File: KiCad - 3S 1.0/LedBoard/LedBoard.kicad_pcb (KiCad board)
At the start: 2 copper layers, 34 x 31.7 mm, 15 parts, among them J1 Conn_01x02, SW1 SW_SPST, U1 TPS565208

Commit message: Finished up LED PCB and made some small tweaks and fixes to main board.
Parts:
- added G***: LOGO, GW_CSSRM3:Sun, F.Cu at (90.0, 28.8)
- D1, D2, D3: value GW CSSRM3.CM-MFN4-A232-1-L -> GW CSSRM1.BM
- R1: value Value: 10K 0805 -> Value: Value: 10K 0805
- moved R2 49.5 mm to (97.0, 44.0), turned to -135 degrees
- moved C5 48.1 mm to (90.0, 45.6)
- moved C6 48.1 mm to (90.0, 43.5)
- moved D1 45.9 mm to (92.9, 39.9), turned to -135 degrees
- moved L1 44.9 mm to (91.6, 52.0), turned to 0 degrees
- moved D2 42.8 mm to (90.0, 37.0), turned to -135 degrees
- moved D3 39.7 mm to (87.1, 34.1), turned to -135 degrees
- moved J1 33.8 mm to (86.1, 22.2), turned to 0 degrees
- moved C1 33.4 mm to (84.6, 51.4), turned to 45 degrees
- moved R1 29.0 mm to (80.1, 51.7), turned to 135 degrees
- moved U1 27.0 mm to (82.5, 49.4), turned to -135 degrees
- moved C2 24.5 mm to (77.9, 49.1), turned to 135 degrees
- moved C3 23.1 mm to (79.4, 47.6), turned to 135 degrees
- moved C4 22.3 mm to (80.8, 46.1), turned to 135 degrees
- moved SW1 16.3 mm to (72.5, 37.0), turned to -90 degrees
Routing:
- net GND: track 1.79 -> 19.4 mm, vias 2 -> 0
- net +12V: track 9.45 -> 26.6 mm
- net Net-(SW1-A): track 11.8 -> 26.1 mm
- net Net-(D1-cathode): track 40.3 -> 52.0 mm, vias 4 -> 0
- net Net-(U1-SW): track 4.56 -> 8.06 mm
- net Net-(D1-anode): track 22.7 -> 25.6 mm
- net Net-(U1-EN): track 4.66 -> 2.58 mm
- removed copper zone on B.Cu, net GND
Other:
- board size 34 x 31.7 mm -> 40 x 40 mm
- rule pad_to_mask_clearance: 0.051 -> 0.005
- rule solder_mask_min_width: 0.09 -> 0.005
- board text added: "Envious.Design OpenTorch V1.0"
- board text added: "env"

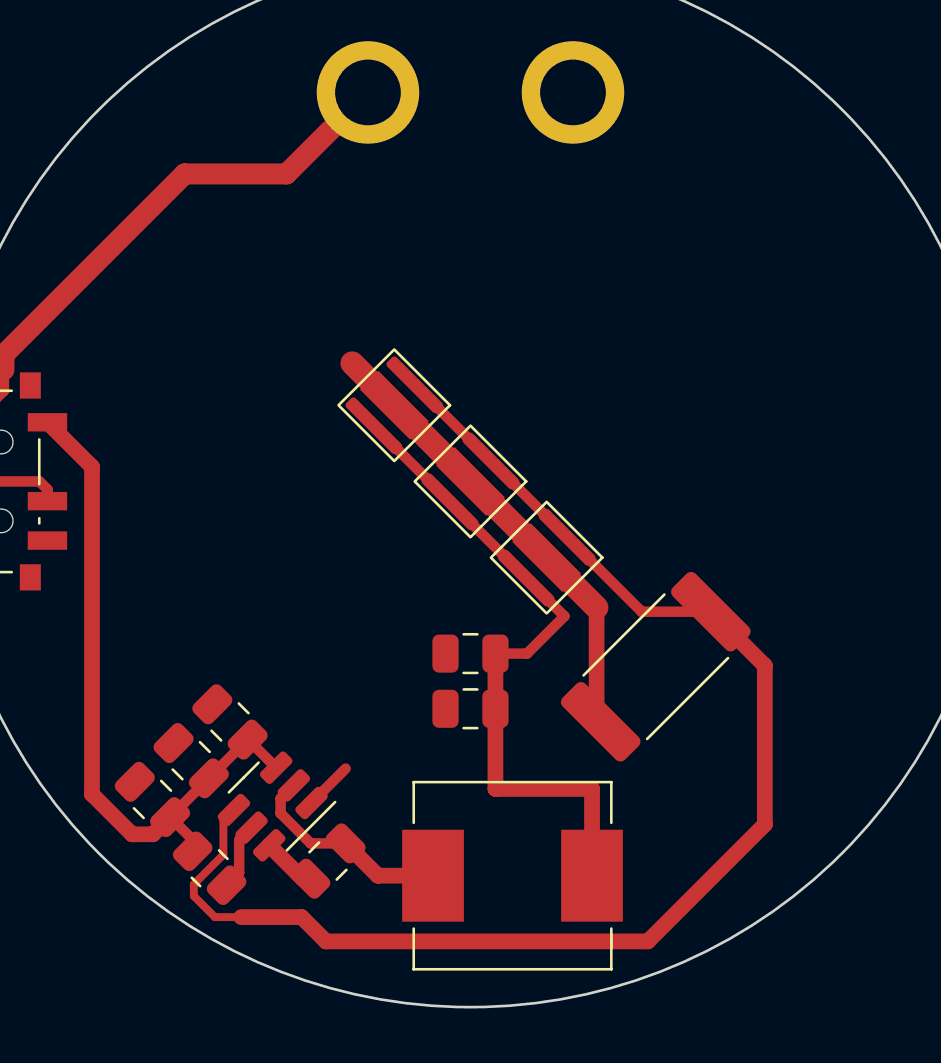
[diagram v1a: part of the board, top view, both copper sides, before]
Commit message: swapped around some parts and re-routed various bits and generated gerbers
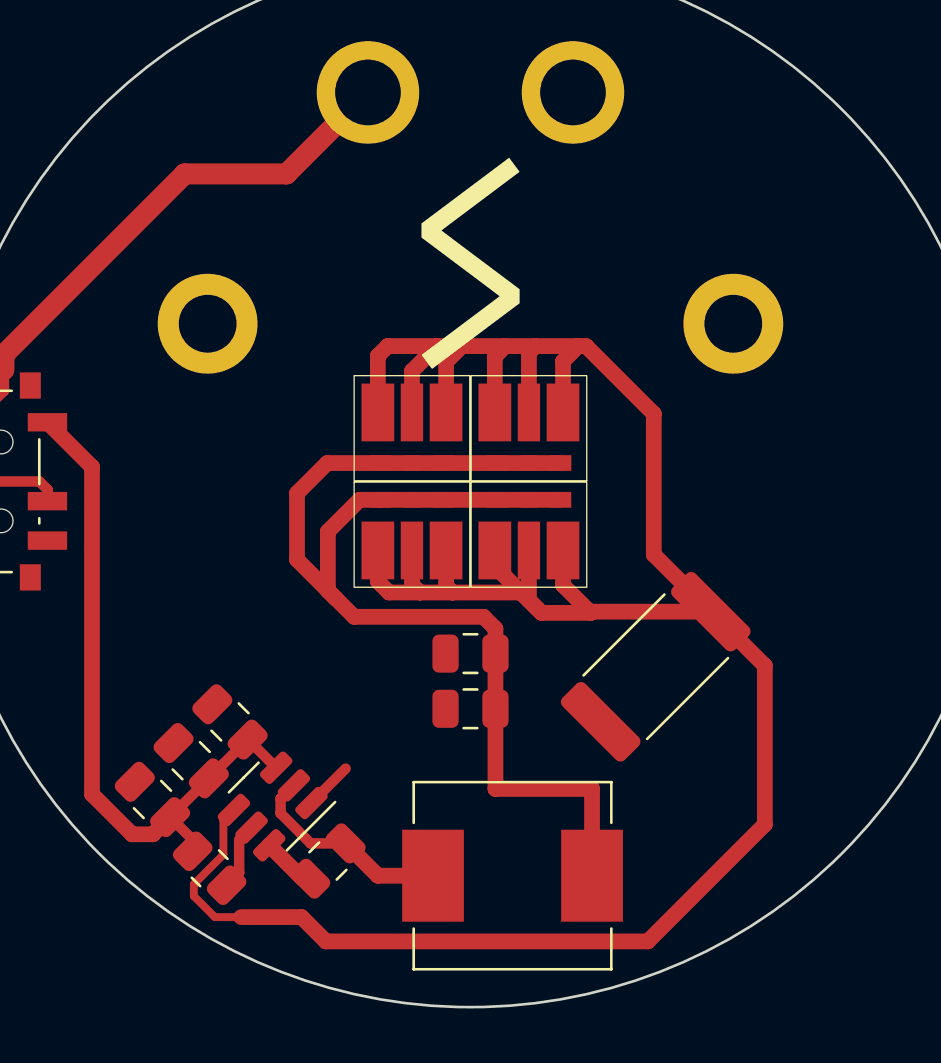
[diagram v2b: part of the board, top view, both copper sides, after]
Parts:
- removed D1, D2, D3: GW CSSRM1.BM, GW_CSSRM3:GW_CSSRM3
- added H1: MountingHole, MountingHole:MountingHole_2.2mm_M2_DIN965_Pad, F.Cu at (80.0, 31.0)
- added H2: MountingHole, MountingHole:MountingHole_2.2mm_M2_DIN965_Pad, F.Cu at (100.0, 31.0)
- added LED1: KW H3L531.TE, KW_H3L531.TE:KW_H3L531.TE, F.Cu at (87.8, 34.4)
- added LED2: KW H3L531.TE, KW_H3L531.TE:KW_H3L531.TE, F.Cu at (87.8, 39.6)
- added LED3: KW H3L531.TE, KW_H3L531.TE:KW_H3L531.TE, F.Cu at (92.2, 39.6)
- added LED4: KW H3L531.TE, KW_H3L531.TE:KW_H3L531.TE, F.Cu at (92.2, 34.4)
- R2: value 170mΩ 2512 -> 190mΩ 2512
- moved G*** 0.18 mm to (90.0, 28.6)
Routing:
- net Net-(U1-VFB): track 52.0 -> 98.6 mm
- net Net-(C5-Pad1): track 25.6 -> 46.8 mm
- net GND: track 19.4 -> 1.85 mm

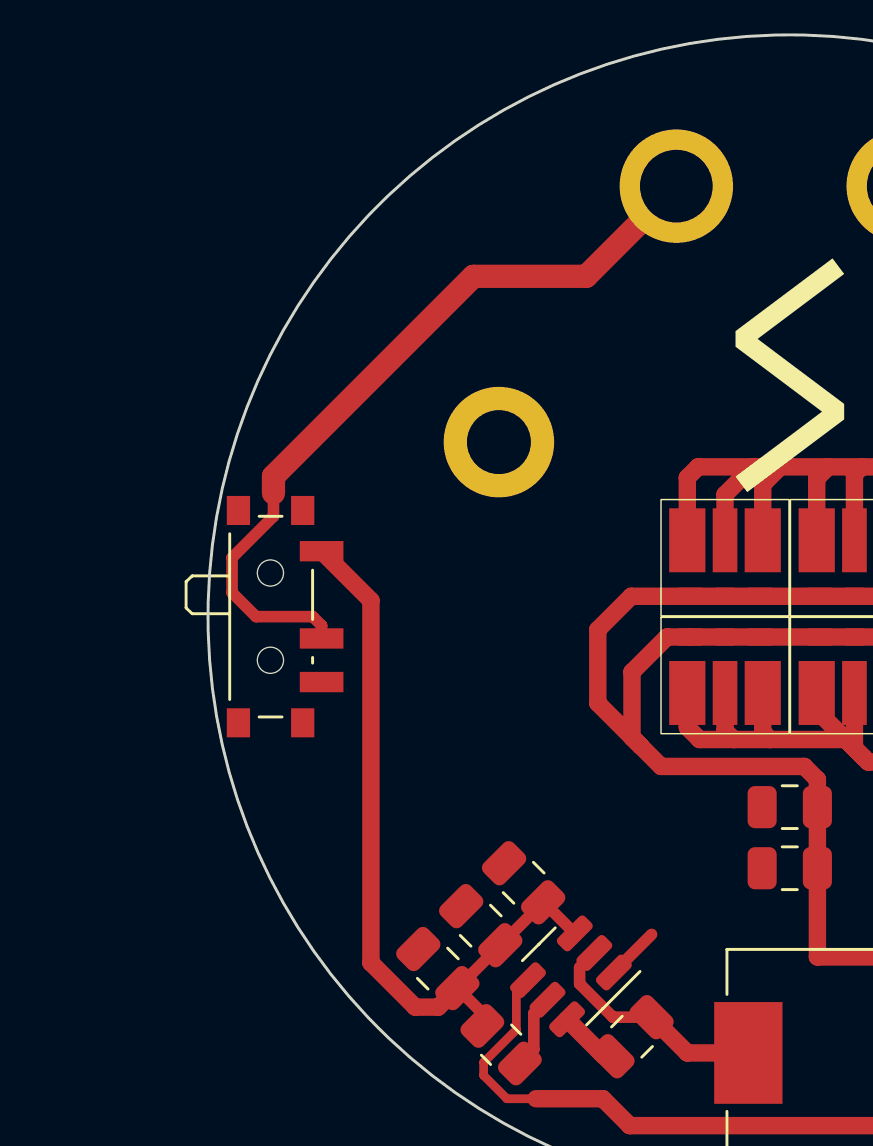
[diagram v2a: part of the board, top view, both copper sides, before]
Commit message: swapped  the switch for pin headers so a switch can be wired externally to the PCB.
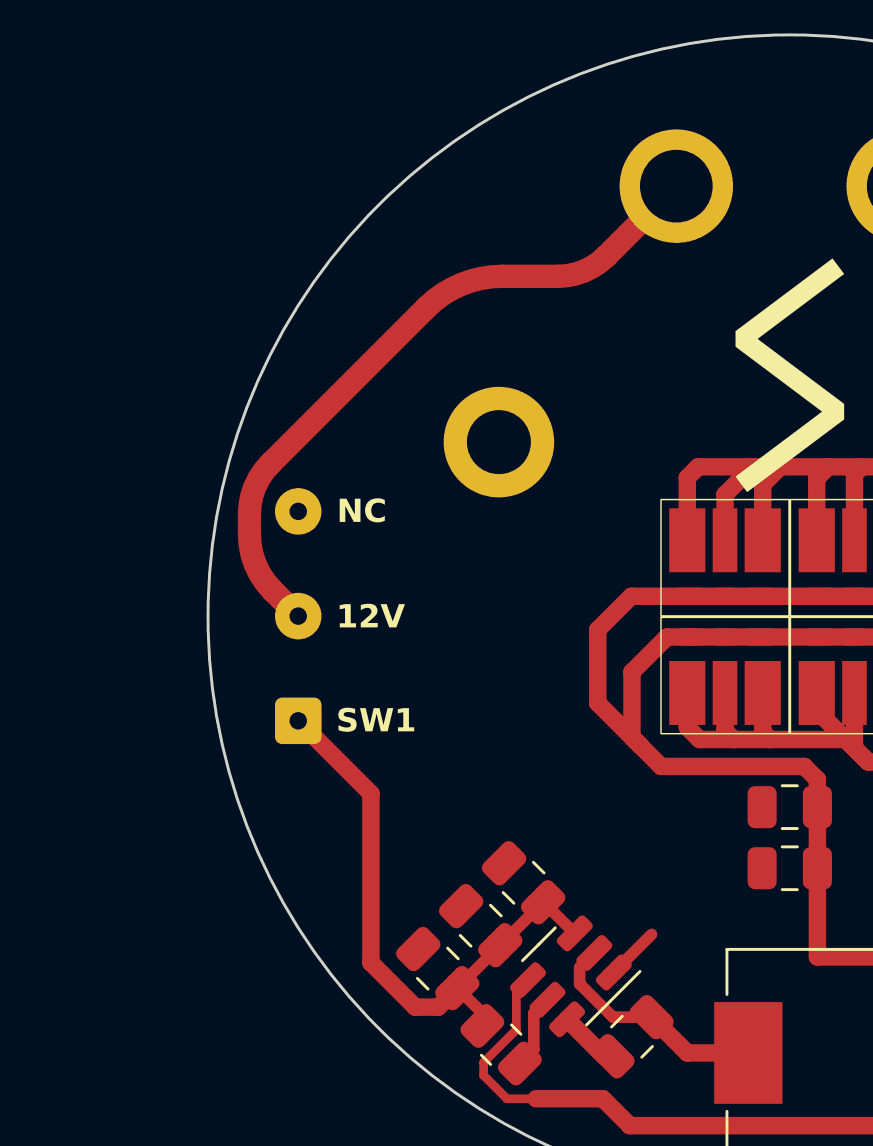
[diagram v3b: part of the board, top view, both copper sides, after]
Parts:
- R1: value Value: Value: 10K 0805 -> Value: 10K 0805
- SW1: footprint Button_Switch_SMD:SW_SPDT_PCM12 -> Connector_Wire:SolderWire-0.1sqmm_1x03_P3.6mm_D0.4mm_OD1mm
- moved SW1 3.64 mm to (73.1, 40.6), turned to 90 degrees
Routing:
- net Net-(SW1-A): track 26.1 -> 20.6 mm
- net +12V: track 26.6 -> 23.6 mm
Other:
- board text added: "12V"
- board text added: "NC"
- board text added: "SW1"

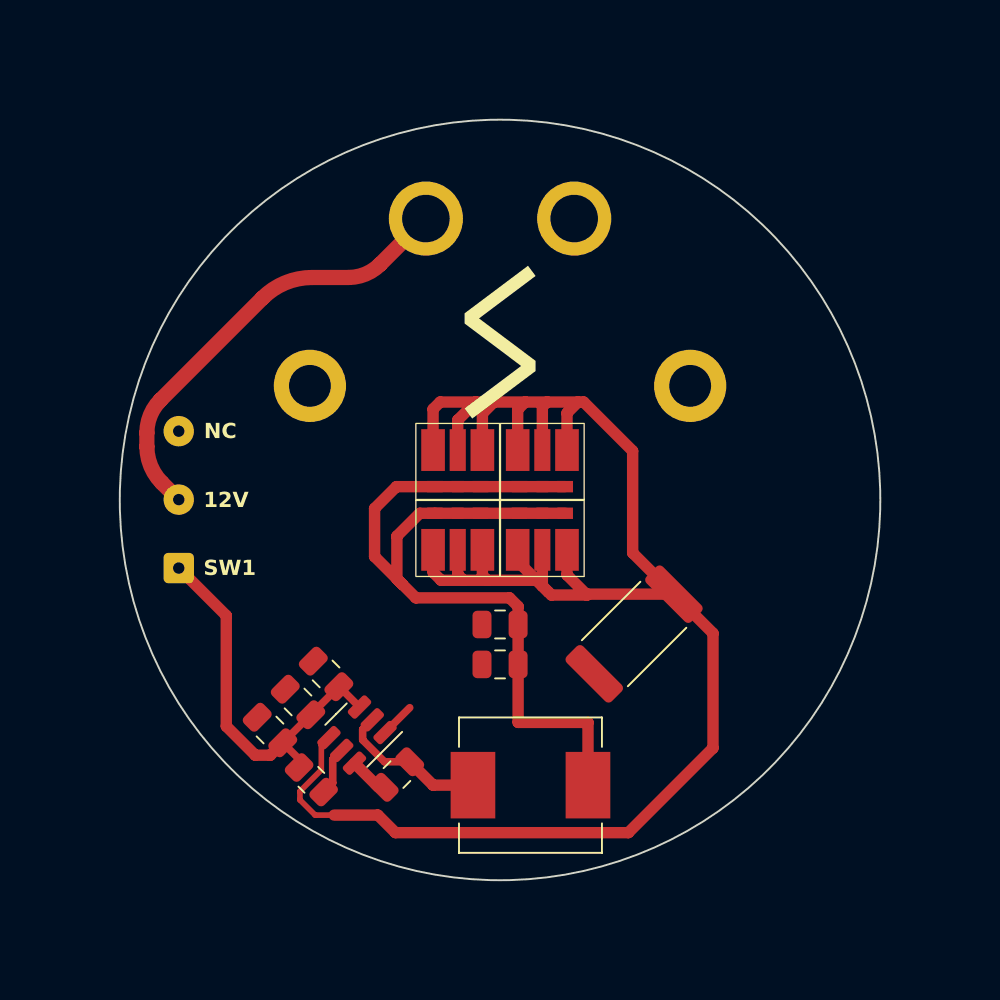
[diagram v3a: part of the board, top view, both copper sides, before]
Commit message: Added new footprint for smaller cheaper, newer led.
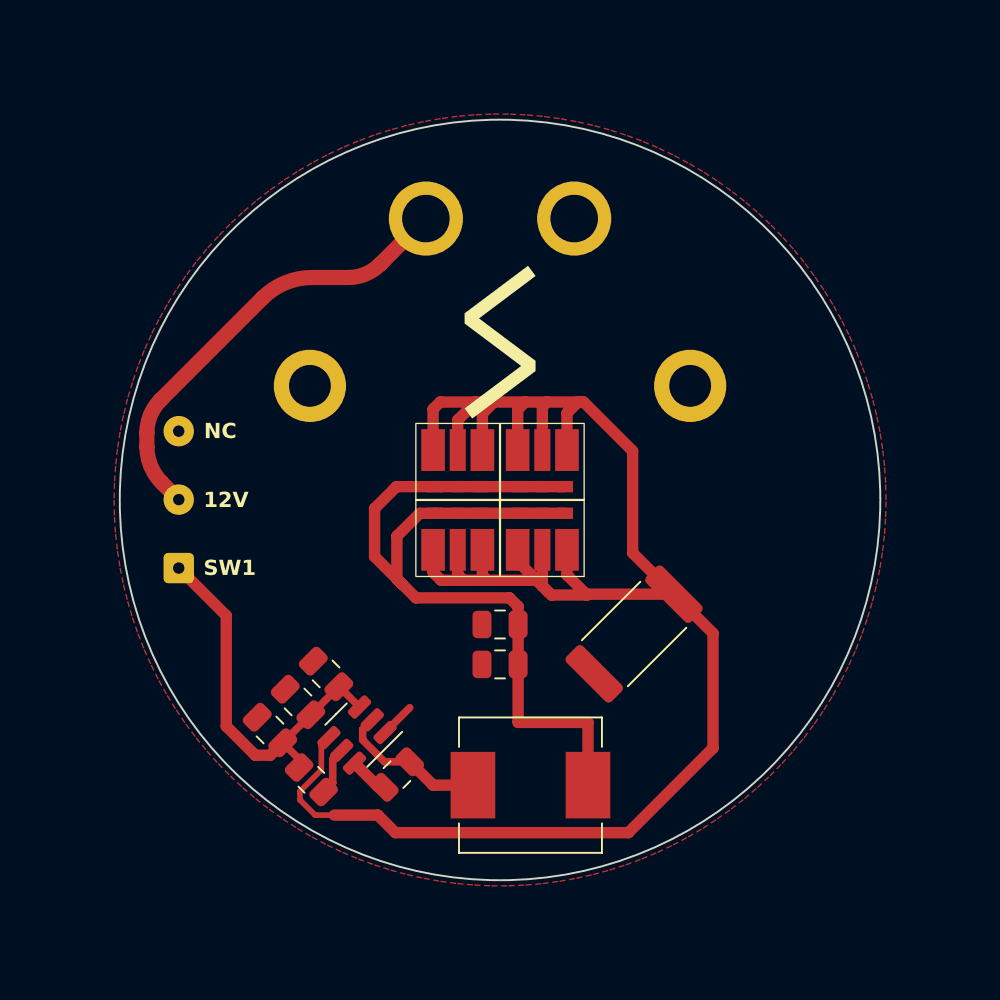
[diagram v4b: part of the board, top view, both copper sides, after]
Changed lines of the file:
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@@
+    )
+  )
+  (zone (net 4) (net_name "GND") (layer "F.Cu") (hatch edge 0.5)
+    (connect_pads yes (clearance 0.15))
+    (min_thickness 0.25) (filled_areas_thickness no)
+    (fill yes (thermal_gap 0.5) (thermal_bridge_width 0.5))
+    (polygon
+      (pts
+        (xy 110.3 37)
+        (xy 110.280131 36.102063)
+        (xy 110.220562 35.205884)
+        (xy 110.121411 34.313217)
+        (xy 109.982872 33.425809)
+        (xy 109.805215 32.545398)
+        (xy 109.588788 31.673707)
+        (xy 109.334015 30.812443)
+        (xy 109.041395 29.963291)
+        (xy 108.711501 29.127914)
+        (xy 108.344978 28.307946)
+        (xy 107.942543 27.504994)
+        (xy 107.504986 26.720629)
+        (xy 107.033161 25.956386)
+        (xy 106.527994 25.213761)
+        (xy 105.990472 24.494209)
+        (xy 105.421648 23.799137)
+        (xy 104.822635 23.129907)
+        (xy 104.194607 22.487828)
+        (xy 103.538791 21.874157)
+        (xy 102.856473 21.290096)
+        (xy 102.148988 20.736787)
+        (xy 101.417721 20.215315)
+        (xy 100.664102 19.726699)
+        (xy 99.889609 19.271897)
+        (xy 99.095756 18.851798)
+        (xy 98.284097 18.467225)
+        (xy 97.456222 18.118932)
+        (xy 96.613752 17.807598)
+        (xy 95.758334 17.533835)
+        (xy 94.891644 17.298177)
+        (xy 94.015379 17.101087)
+        (xy 93.131253 16.94295)
+        (xy 92.240998 16.824076)
+        (xy 91.346356 16.744696)
+        (xy 90.449078 16.704968)
+        (xy 89.550922 16.704968)
+        (xy 88.653644 16.744696)
+        (xy 87.759002 16.824076)
+        (xy 86.868747 16.94295)
+        (xy 85.984621 17.101087)
+        (xy 85.108356 17.298177)
+        (xy 84.241666 17.533835)
+        (xy 83.386248 17.807598)
+        (xy 82.543778 18.118932)
+        (xy 81.715903 18.467225)
+        (xy 80.904244 18.851798)
+        (xy 80.110391 19.271897)
+        (xy 79.335898 19.726699)
+        (xy 78.582279 20.215315)
+        (xy 77.851012 20.736787)
+        (xy 77.143527 21.290096)
+        (xy 76.461209 21.874157)
+        (xy 75.805393 22.487828)
+        (xy 75.177365 23.129907)
+        (xy 74.578352 23.799137)
+        (xy 74.009528 24.494209)
+        (xy 73.472006 25.213761)
+        (xy 72.966839 25.956386)
+        (xy 72.495014 26.720629)
+        (xy 72.057457 27.504994)
+        (xy 71.655022 28.307946)
+        (xy 71.288499 29.127914)
+        (xy 70.958605 29.963291)
+        (xy 70.665985 30.812443)
+        (xy 70.411212 31.673707)
+        (xy 70.194785 32.545398)
+        (xy 70.017128 33.425809)
+        (xy 69.878589 34.313217)
+        (xy 69.779438 35.205884)
+        (xy 69.719869 36.102063)
+        (xy 69.7 37)
+        (xy 69.719869 37.897937)
+        (xy 69.779438 38.794116)
+        (xy 69.878589 39.686783)
+        (xy 70.017128 40.574191)
+        (xy 70.194785 41.454602)
+        (xy 70.411212 42.326293)
+        (xy 70.665985 43.187557)
+        (xy 70.958605 44.036709)
+        (xy 71.288499 44.872086)
+        (xy 71.655022 45.692054)
+        (xy 72.057457 46.495006)
+        (xy 72.495014 47.279371)
+        (xy 72.966839 48.043614)
+        (xy 73.472006 48.786239)
+        (xy 74.009528 49.505791)
+        (xy 74.578352 50.200863)
+        (xy 75.177365 50.870093)
+        (xy 75.805393 51.512172)
+        (xy 76.461209 52.125843)
+        (xy 77.143527 52.709904)
+        (xy 77.851012 53.263213)
+        (xy 78.582279 53.784685)
+        (xy 79.335898 54.273301)
+        (xy 80.110391 54.728103)
+        (xy 80.904244 55.148202)
+        (xy 81.715903 55.532775)
+        (xy 82.543778 55.881068)
+        (xy 83.386248 56.192402)
+        (xy 84.241666 56.466165)
+        (xy 85.108356 56.701823)
+        (xy 85.984621 56.898913)
+        (xy 86.868747 57.05705)
+        (xy 87.759002 57.175924)
+        (xy 88.653644 57.255304)
+        (xy 89.550922 57.295032)
+        (xy 90.449078 57.295032)
+        (xy 91.346356 57.255304)
+        (xy 92.240998 57.175924)
+        (xy 93.131253 57.05705)
+        (xy 94.015379 56.898913)
+        (xy 94.891644 56.701823)
+        (xy 95.758334 56.466165)
+        (xy 96.613752 56.192402)
+        (xy 97.456222 55.881068)
+        (xy 98.284097 55.532775)
+        (xy 99.095756 55.148202)
+        (xy 99.889609 54.728103)
+        (xy 100.664102 54.273301)
+        (xy 101.417721 53.784685)
+        (xy 102.148988 53.263213)
+        (xy 102.856473 52.709904)
+        (xy 103.538791 52.125843)
+        (xy 104.194607 51.512172)
+        (xy 104.822635 50.870093)
+        (xy 105.421648 50.200863)
+        (xy 105.990472 49.505791)
+        (xy 106.527994 48.786239)
+        (xy 107.033161 48.043614)
+        (xy 107.504986 47.279371)
+        (xy 107.942543 46.495006)
+        (xy 108.344978 45.692054)
+        (xy 108.711501 44.872086)
+        (xy 109.041395 44.036709)
+        (xy 109.334015 43.187557)
+        (xy 109.588788 42.326293)
+        (xy 109.805215 41.454602)
+        (xy 109.982872 40.574191)
+        (xy 110.121411 39.686783)
+        (xy 110.220562 38.794116)
+        (xy 110.280131 37.897937)
+        (xy 110.3 37)
+      )
     )
   )
